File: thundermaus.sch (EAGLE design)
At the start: 46 parts, among them IC1 LM7805, IC2 TINY24/44/84-PU, Q1 FGH20N60SFD, Q2 2n7000, Q3 2n7000, X1 TOBU3

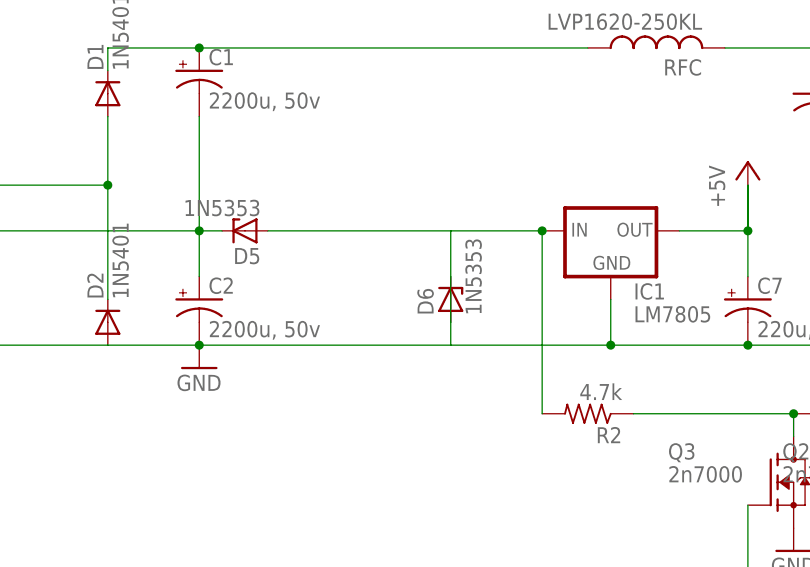
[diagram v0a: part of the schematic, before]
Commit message: merge v2 changes; drop D6, move few things subtly
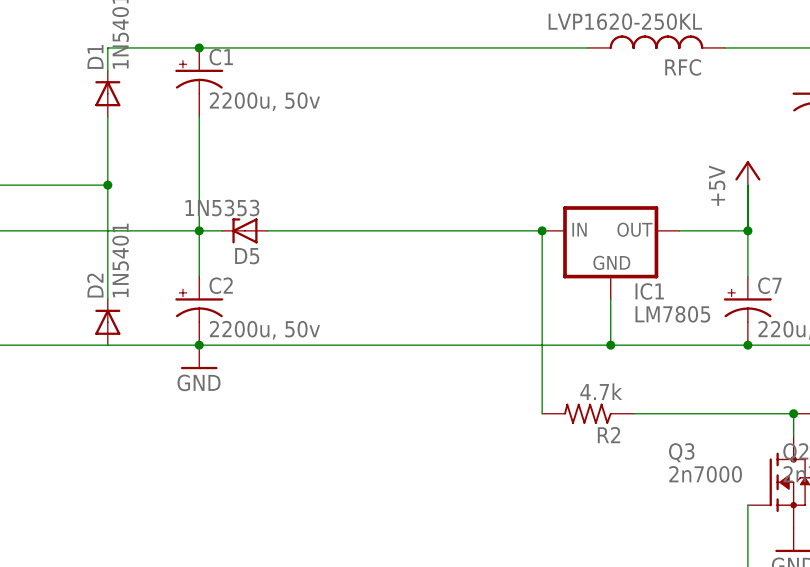
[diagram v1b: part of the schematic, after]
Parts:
- removed D6: 1N5353, diode:1N5333
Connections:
- new net N$2: D5.A, IC1.IN, R2.2
- net GND: no longer D5.A, D6.A, D6.C, IC1.IN, R2.2
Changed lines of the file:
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@@
 <part name="VR1" library="pot2" deviceset="PTV09" device="" value=""/>
 <part name="VR2" library="pot2" deviceset="PTV09" device="" value=""/>
-<part name="D6" library="diode" deviceset="1N5333" device="" value="1N5353"/>
 <part name="D7" library="diode" deviceset="1N5333" device="" value="1N5353"/>
 <part name="LED2" library="led" deviceset="LED" device="5MM"/>
@@
 <instance part="VR1" gate="&gt;NAME" x="137.16" y="-25.4" rot="MR0"/>
 <instance part="VR2" gate="&gt;NAME" x="162.56" y="-25.4" rot="MR0"/>
-<instance part="D6" gate="1" x="58.42" y="48.26" rot="R90"/>
 <instance part="D7" gate="1" x="22.86" y="-12.7" rot="R90"/>
 <instance part="LED2" gate="G$1" x="12.7" y="-15.24"/>
@@
 <wire x1="91.44" y1="43.18" x2="76.2" y2="43.18" width="0.1524" layer="91"/>
 <wire x1="76.2" y1="48.26" x2="76.2" y2="43.18" width="0.1524" layer="91"/>
-<wire x1="76.2" y1="43.18" x2="58.42" y2="43.18" width="0.1524" layer="91"/>
-<wire x1="58.42" y1="43.18" x2="30.48" y2="43.18" width="0.1524" layer="91"/>
+<wire x1="76.2" y1="43.18" x2="30.48" y2="43.18" width="0.1524" layer="91"/>
 <wire x1="20.32" y1="43.18" x2="30.48" y2="43.18" width="0.1524" layer="91"/>
 <wire x1="121.92" y1="43.18" x2="132.08" y2="43.18" width="0.1524" layer="91"/>
@@
 <pinref part="GND" gate="-1" pin="1"/>
 <wire x1="0" y1="43.18" x2="20.32" y2="43.18" width="0.1524" layer="91"/>
-<wire x1="38.1" y1="55.88" x2="58.42" y2="55.88" width="0.1524" layer="91"/>
-<wire x1="58.42" y1="55.88" x2="68.58" y2="55.88" width="0.1524" layer="91"/>
-<wire x1="68.58" y1="55.88" x2="68.58" y2="35.56" width="0.1524" layer="91"/>
-<junction x="68.58" y="55.88"/>
-<pinref part="D5" gate="1" pin="A"/>
-<pinref part="IC1" gate="1" pin="IN"/>
-<pinref part="R2" gate="G$1" pin="2"/>
-<pinref part="D6" gate="1" pin="C"/>
-<wire x1="58.42" y1="50.8" x2="58.42" y2="55.88" width="0.1524" layer="91"/>
-<pinref part="D6" gate="1" pin="A"/>
-<wire x1="58.42" y1="50.8" x2="58.42" y2="45.72" width="0.1524" layer="91"/>
-<wire x1="58.42" y1="45.72" x2="58.42" y2="43.18" width="0.1524" layer="91"/>
 </segment>
 <segment>
@@
 </segment>
 </net>
+<net name="N$2" class="0">
+<segment>
+<pinref part="R2" gate="G$1" pin="2"/>
+<wire x1="68.58" y1="55.88" x2="68.58" y2="35.56" width="0.1524" layer="91"/>
+<junction x="68.58" y="55.88"/>
+<pinref part="IC1" gate="1" pin="IN"/>
+<wire x1="38.1" y1="55.88" x2="68.58" y2="55.88" width="0.1524" layer="91"/>
+<pinref part="D5" gate="1" pin="A"/>
+</segment>
+</net>

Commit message: name all the things
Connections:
- net +5V renamed 5V
- net N$1 renamed LED2-P
- net N$10 renamed LED3-P
- net N$11 renamed GATE
- net N$12 renamed LEDP
- net N$13 renamed MISO
- net N$14 renamed SCK
- net N$15 renamed RST
- net N$17 renamed PA3
- net N$18 renamed LED
- net N$19 renamed COLLECTOR
- net N$2 renamed 16V
- net N$20 renamed LVAC2
- net N$21 renamed AUDIO-IN
- net N$22 renamed AUDIO
- net N$23 renamed LVAC1
- net N$24 renamed PA7
- net N$3 renamed PB2
- net N$4 renamed 70VDC
- net N$5 renamed HVDC
- net N$6 renamed PULLUP_DISABLE
- net N$7 renamed RESONANT
- net N$8 renamed PB1
- net N$9 renamed MOSI
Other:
- moved on the sheet: D3, D5, R3, R5
